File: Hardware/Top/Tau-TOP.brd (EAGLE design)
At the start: 38 x 38 mm, 64 parts, among them U3 PCF8523, U4 NRF52832_MODULE_MDBT42, U5 FT231XS

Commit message: Changes committed to top and bottom board
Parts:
- added J1: (no value), LinnesLab-Connectors:1X07
- moved C25 13.6 mm to (21.7, 36.0)
- moved R3 12.3 mm to (11.7, 17.0)
- moved C11 7.56 mm to (16.2, 24.9), turned to 270 degrees
- moved L2 7.42 mm to (15.5, 31.5)
- moved C9 5.77 mm to (23.6, 24.9)
- moved R4 5.77 mm to (11.0, 31.5), turned to 180 degrees
- moved C20 5.36 mm to (17.9, 25.1)
- moved C8 4.26 mm to (11.9, 24.8)
- moved C12 4.19 mm to (13.4, 24.8)
- moved C10 4.14 mm to (14.7, 24.8)
- moved C7 4.05 mm to (10.6, 24.8)
- moved XTAL2 2.28 mm to (25.1, 16.9)
- moved C21 1.47 mm to (18.7, 16.6)
- moved U2 0.26 mm to (19.1, 20.9)
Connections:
- removed net BATT: R13.1, R14.2
- removed net CD1: SD2.CD1
- removed net CHRG.STAT: CHRG2.1, R12.1
- removed net CS.OLED: U2.13
- removed net DC.OLED: U2.15
- removed net RESET.OLED: U2.14
- removed net SD.CS: SD2.2
- removed net SW1: U$1.A1, U$2.A1
- new net A4/BATT: R13.1, R14.2, U4.5
- new net A6/TIA: U4.7
- new net A7/PPG: U4.8
- new net D11/SW1: U$1.A1, U4.25
- new net D15/SW2: U$2.A1, U4.29
- new net D16/CS.OLED: U2.13, U4.30
- new net D27/CHRG.STATUS: CHRG2.1, R12.1, U4.4
- new net D29/LED.CTRL: U4.6
- new net D3/RESET.OLED: U2.14, U4.16
- new net D4/DC.OLED: U2.15, U4.17
- new net D5/CD1: SD2.CD1, U4.18
- new net D7/SD.CS: SD2.2, U4.20

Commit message: Changes made to top and bottom board
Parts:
- removed C22: (no value), LinnesLab-Passives:C0603
- removed C23, C24: 300p, LinnesLab-Passives:C0603
- removed C25: 10u, LinnesLab-Passives:C0805
- removed C26: 100n, LinnesLab-Passives:C0603
- removed CHRG2: MCP73831, LinnesLab-Power:SOT23-5
- removed D4, D5: (no value), LinnesLab-DiscreteSemi:USC
- removed JP2: (no value), LinnesLab-Switches:SMT-JUMPER_2_NO_SILK
- removed LDO2: MIC5504, LinnesLab-Power:SOT23-5
- removed LED5: RED, LinnesLab-LED:LED-0603
- removed LED6: YELLOW, LinnesLab-LED:LED-0603
- removed R19, R20: 1k, LinnesLab-Passives:R0603
- removed U$2: SWITCH.MOM, LinnesLab-Switches:TACTILE_SWITCH_SMD_6.2MM_TALL
- removed U5: FT231XS, LinnesLab-DigitalIC:SSOP20_L
- removed XTAL3: 32.7680kHz, LinnesLab-Clocks:2-SMD.NOLEAD.2.0MMTO1.2MM
- added C1, C18, C19: 1u, LinnesLab-Passives:C0603
- added C3: (no value), LinnesLab-Passives:C0603
- added C4: 10uF, LinnesLab-Passives:C0603
- added CHRG1: MCP73831, LinnesLab-Power:SOT23-5
- added D2, D3: (no value), LinnesLab-DiscreteSemi:USC
- added JP1: (no value), LinnesLab-Switches:SMT-JUMPER_2_NO_SILK
- added LDO1: MIC5504, LinnesLab-Power:SOT23-5
- added LED1: RED, LinnesLab-LED:LED-0603
- added LED2: BLUE, LinnesLab-LED:LED-0603
- added R16: 100k, LinnesLab-Passives:R0603
- added R7: 27, LinnesLab-Passives:R0603
- added SW1: (no value), LinnesLab-Switches:BUTTON-GULLWING
- added XTAL1: 32.768kHz, LinnesLab-Clocks:2-SMD.NOLEAD.2.0MMTO1.2MM
- C11, C12: value 2.2uF -> 300p; device LinnesLab-Passives:C0402 -> LinnesLab-Passives:C0603
- C13, C14: value 4.7u -> 47p
- C16: value 47p -> 4.7u
- C17: value 47p -> 100n
- C2: value 1u -> 10u; device LinnesLab-Passives:C0603 -> LinnesLab-Passives:C0805
- C21: value (none) -> 4.7u
- C5, C6: value 1u -> 2.2uF; device LinnesLab-Passives:C0603 -> LinnesLab-Passives:C0402
- C7: value 2.2uF -> (none); device LinnesLab-Passives:C0402 -> LinnesLab-Passives:C0603
- C9: value 10uF -> 2.2uF; device LinnesLab-Passives:C0603 -> LinnesLab-Passives:C0402
- J1: device LinnesLab-Connectors:1X07 -> LinnesLab-Connectors:1X07_1.27MM
- LED4: value BLUE -> YELLOW
- R1, R2: value 0 -> 10k
- R13: value 100k -> 1k
- R14, R15: value 100k -> 0
- R17: value 27 -> 100k
- R18: value 27 -> 1k
- R5, R6: value 10k -> 1k
- R8: value 1k -> 27
- R9: value 1k -> 100k
- SW3: value (none) -> SWITCH.MOM; device LinnesLab-Switches:BUTTON-GULLWING -> LinnesLab-Switches:TACTILE_SWITCH_SMD_6.2MM_TALL
- U4: value NRF52832_MODULE_MDBT42 -> FT231XS; device LinnesLab-Microcontrollers:BLE_MODULE_RAYTAC_MDBT42 -> LinnesLab-DigitalIC:SSOP20_L
- XTAL2: value 32.768kHz -> 32.7680kHz
- moved R6 66.4 mm to (41.3, 27.9), turned to 180 degrees
- moved R5 62.7 mm to (41.3, 25.9), turned to 180 degrees
- moved J1 62.6 mm to (5.00, 33.0)
- moved D1 55.8 mm to (12.8, -20.9), turned to 0 degrees
- moved R9 50.8 mm to (7.54, -11.4)
- moved C20 47.9 mm to (21.3, -22.7)
- moved R13 46.5 mm to (46.7, -12.2), turned to 0 degrees
- moved C2 42.6 mm to (21.7, 36.0), turned to 0 degrees
- moved XTAL2 42.6 mm to (31.8, -25.1), turned to 90 degrees
- moved U4 38.9 mm to (36.1, -9.35), turned to 90 degrees
- moved C16 37.9 mm to (5.00, -10.4), turned to 90 degrees
- moved SW3 37.8 mm to (22.2, 4.09)
- moved LED4 36.6 mm to (46.7, -8.43)
- moved R8 32.6 mm to (30.7, -5.51), turned to 0 degrees
- moved R15 30.9 mm to (-4.85, -20.1), turned to 0 degrees
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- renumbered CORTEX1 to DEBUG1, L2 to L1, SD2 to SD1, U$1 to SW2, USB2 to USB1
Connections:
- removed net FRST: U4.38
- net !CTS: now also JP1.2, U4.9; no longer JP2.2, U5.9
- net 3.3V: now also C17.2, C19.1, C2.2, C20.1, C9.2, D3.-, J1.4, LDO1.5, LED3.A, LED4.A, R1.2, R12.2, R2.2, U4.14, U4.3; no longer C12.2, C15.2, C2.1, C25.2, C6.1, D1.-, LDO2.5, LED5.A, LED6.A, R15.2, R5.2, R6.2, U4.11, U5.14, U5.3
- net A4/BATT: now also R16.1, R17.2; no longer R13.1, R14.2, U4.5
- net A6/TIA: now also J1.6; no longer U4.7
- net A7/PPG: now also J1.7; no longer U4.8
- net D11/SW1: no longer U4.25
- net D15/SW2: now also SW3.A1; no longer U$2.A1, U4.29
- net D16/CS.OLED: no longer U4.30
- net D27/CHRG.STATUS: now also CHRG1.1, R9.1; no longer CHRG2.1, R12.1, U4.4
- net D29/LED.CTRL: now also J1.5; no longer U4.6
- net D3/RESET.OLED: no longer U4.16
- net D4/DC.OLED: no longer U4.17
- net D5/CD1: no longer U4.18
- net D7/SD.CS: no longer U4.20
- net DFU: now also SW1.3; no longer SW3.3, U4.34
- net DTR: now also C15.1, U4.1; no longer C26.1, U5.1
- net FT3V3: now also U4.13; no longer U5.13
- net GND: now also C1.2, C11.2, C12.2, C13.1, C14.2, C16.1, C18.1, C19.2, C2.1, C21.2, C3.1, C4.1, C6.1, C7.2, CHRG1.2, J1.3, JP1.1, LDO1.2, LED1.C, LED2.C, R12.1, R17.1, SW1.1, SW3.B1, SW3.B2, U4.16, U4.6; no longer C11.1, C12.1, C13.2, C14.1, C15.1, C16.2, C2.2, C21.1, C22.2, C23.2, C24.2, C25.1, C5.1, C6.2, CHRG2.2, JP2.1, LDO2.2, LED3.C, LED4.C, R14.1, R15.1, SW3.1, U$2.B1, U$2.B2, U4.1, U4.12, U4.24, U4.39, U5.16, U5.6
- net LED1: now also R5.2; no longer R8.2, U4.31
- net LED2: now also R6.2; no longer R9.2, U4.33
- net MISO: no longer U4.28
- net MOSI: no longer U4.27
- net N$10: now also CHRG1.5; no longer CHRG2.5
- net N$12: now also XTAL2.P$1; no longer XTAL3.P$1
- net N$13: now also XTAL2.P$2; no longer XTAL3.P$2
- net N$16: now also C3.2, XTAL1.P$1; no longer C21.2, U4.13, XTAL2.P$1
- net N$17: now also C7.1, XTAL1.P$2; no longer C22.1, U4.14, XTAL2.P$2
- net N$18: now also LED1.A, R5.1; no longer LED3.A, R8.1
- net N$19: now also LED2.A, R6.1; no longer LED4.A, R9.1
- net N$20: no longer U4.10
- net N$21: now also C1.1; no longer C20.1, U4.9
- net N$22: now also R7.2, U4.12; no longer R17.2, U5.12
- net N$24: now also R8.2, U4.11; no longer R18.2, U5.11
- net N$25: now also LED3.C, R13.2; no longer LED5.C, R19.2
- net N$26: now also LED4.C, R18.2; no longer LED6.C, R20.2
- net N$3: now also C8.2; no longer C7.2
- net N$4: now also C8.1; no longer C7.1
- net N$5: now also C5.2; no longer C8.2
- net N$6: now also C5.1; no longer C8.1
- net N$7: now also C4.2; no longer C9.2
- net N$8: now also C6.2; no longer C11.2
- net P0.09/NFC1: now also C11.1; no longer C24.1, U4.22
- net P0.10/NFC2: now also C12.1; no longer C23.1, U4.23
- net RESET: now also C15.2, D3.+; no longer C26.2, D1.+, U4.35
- net RXD.FT: now also R15.1, U4.4; no longer R2.1, U5.4
- net RXD.NRF: now also R14.2; no longer R1.2, U4.21
- net RXLED: now also R13.1, U4.17; no longer R19.1, U5.17
- net SCK: no longer U4.26
- net SCL: now also J1.2, R2.1; no longer R6.1, U4.3
- net SDA: now also J1.1, R1.1; no longer R5.1, U4.2
- net SWCLK: no longer U4.36
- net SWDIO: no longer U4.37
- net SWO: no longer U4.32
- net TXD.FT: now also R14.1, U4.20; no longer R1.1, U5.20
- net TXD.NRF: now also R15.2; no longer R2.2, U4.19
- net TXLED: now also R18.1, U4.10; no longer R20.1, U5.10
- net USB+: now also C14.1, R8.1; no longer C16.1, R18.1
- net USB-: now also C13.2, R7.1; no longer C17.2, R17.1
- net VIN: now also C16.2, C18.2, CHRG1.4, D1.-, D2.-, LDO1.1, LDO1.3, R9.2; no longer C14.2, C5.2, CHRG2.4, D4.-, D5.-, LDO2.1, LDO2.3, R12.2
- net VLIPO: now also C21.1, CHRG1.3, D1.+, R16.2; no longer C13.1, CHRG2.3, D4.+, R13.2
- net V_USB: now also D2.+, U4.15; no longer D5.+, U5.15
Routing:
- net N$13: track 0.00 -> 2.00 mm
- net N$12: track 0.00 -> 1.96 mm
- added copper zone on layer 16, net GND

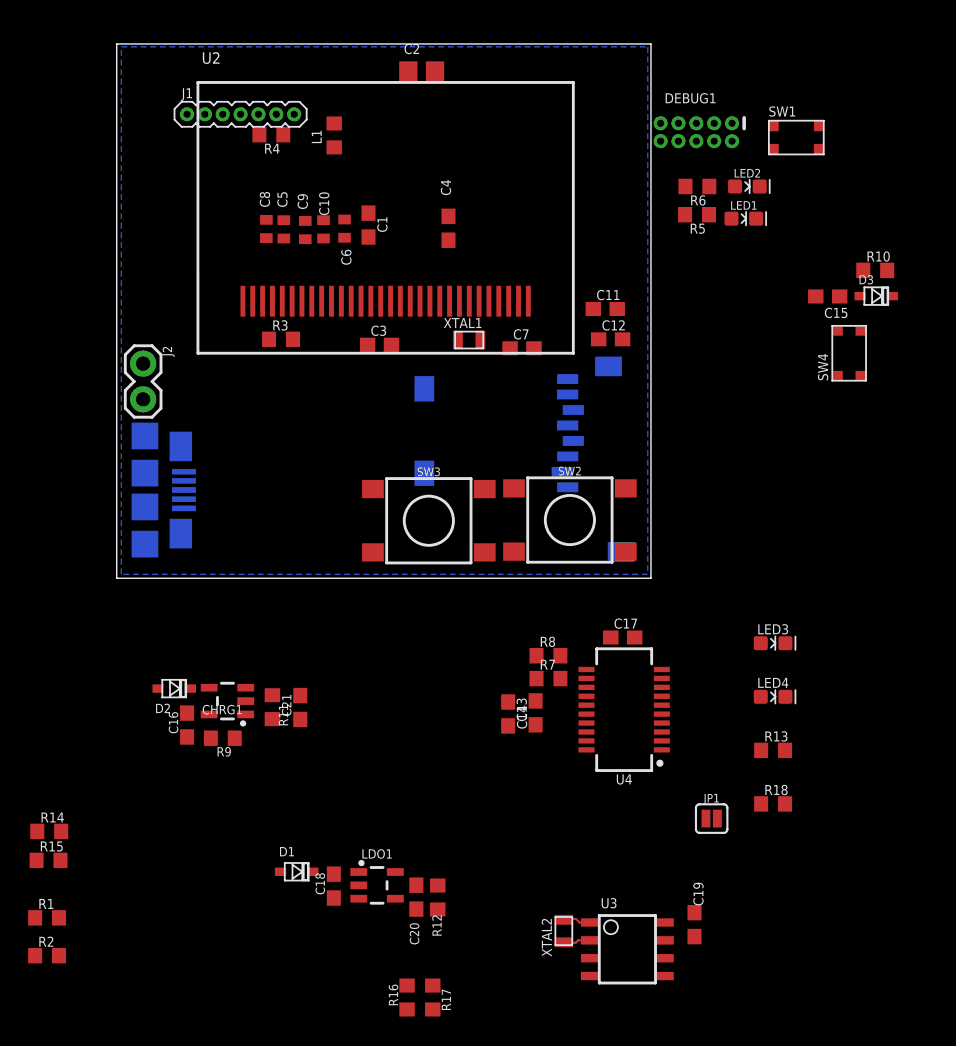
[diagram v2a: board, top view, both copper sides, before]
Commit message: Changes made to Top board and arduino files
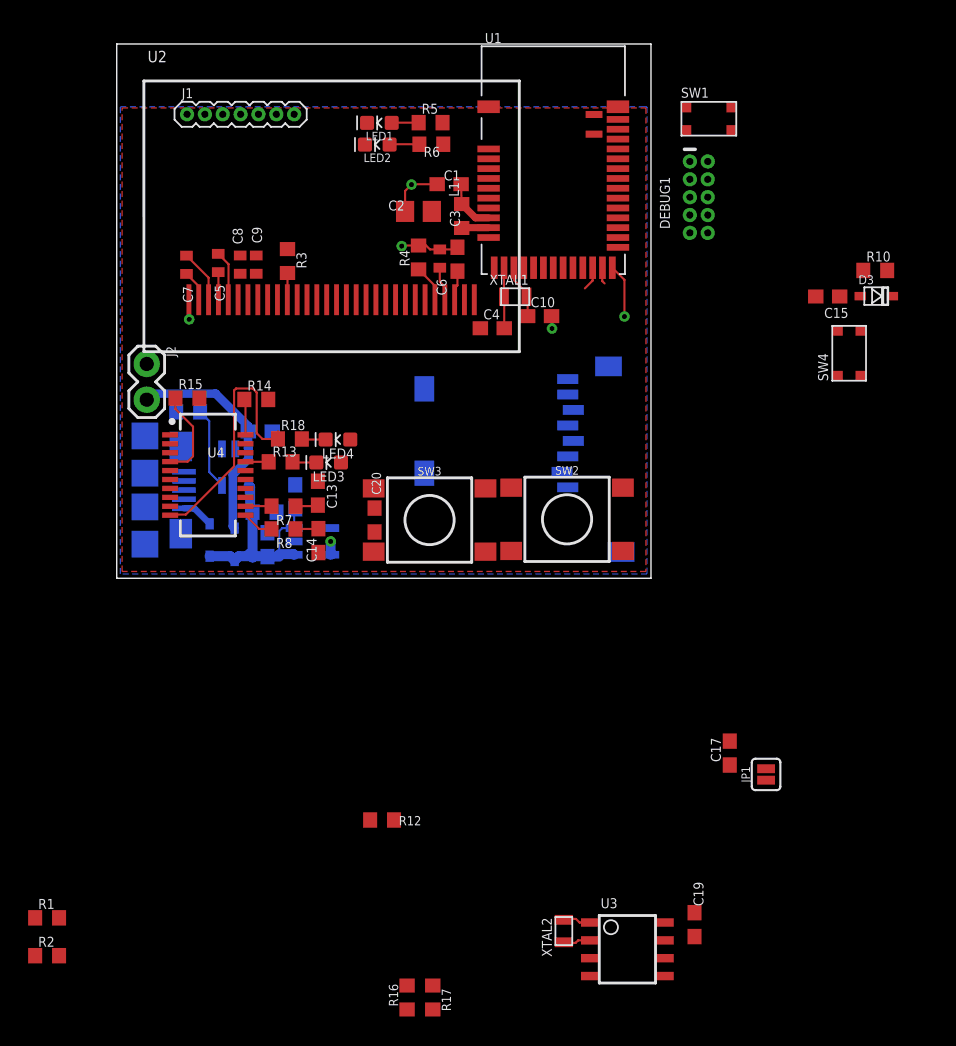
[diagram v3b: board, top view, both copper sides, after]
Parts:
- removed C11, C12: 300p, LinnesLab-Passives:C0603
- added U1: NRF52832_MODULE_MDBT42, LinnesLab-Microcontrollers:BLE_MODULE_RAYTAC_MDBT42
- C10: value 2.2uF -> (none); device LinnesLab-Passives:C0402 -> LinnesLab-Passives:C0603
- C3: value (none) -> 10uF
- C4: value 10uF -> (none)
- C7: value (none) -> 2.2uF; device LinnesLab-Passives:C0603 -> LinnesLab-Passives:C0402
- moved R18 43.1 mm to (12.3, 9.91)
- moved R13 40.6 mm to (11.7, 8.28)
- moved LED4 36.0 mm to (15.7, 9.87), turned to 180 degrees
- moved R15 34.3 mm to (5.03, 12.8)
- moved LED3 34.1 mm to (15.1, 8.23), turned to 180 degrees
- moved R14 34.1 mm to (9.93, 12.7)
- moved U4 34.0 mm to (6.48, 7.34), turned to 270 degrees
- moved C20 27.0 mm to (18.3, 4.14), turned to 90 degrees
- moved LED1 26.8 mm to (18.7, 32.4), turned to 180 degrees
- moved LED2 26.5 mm to (18.5, 30.8), turned to 180 degrees
- moved LDO1 24.9 mm to (13.9, 2.62), flipped to the bottom, turned to 90 degrees
- moved C18 24.7 mm to (10.7, 2.39), flipped to the bottom, turned to 270 degrees
- moved C7 24.6 mm to (4.96, 22.3), turned to 270 degrees
- moved D1 23.7 mm to (8.38, 2.41), flipped to the bottom, turned to 270 degrees
- moved R7 22.5 mm to (11.9, 5.13), turned to 180 degrees
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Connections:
- removed net N$16: C3.2, XTAL1.P$1
- removed net N$17: C7.1, XTAL1.P$2
- removed net N$20: L1.1
- removed net N$21: C1.1, L1.2
- new net FRST: U1.38
- new net N$31: C4.2, U1.13, XTAL1.P$1
- new net N$32: C10.1, U1.14, XTAL1.P$2
- new net N$35: L1.1, U1.10
- new net N$36: C1.1, L1.2, U1.9
- new net RXD: U1.21
- new net TXD: U1.19
- net 3.3V: now also C8.2, U1.11; no longer C10.2
- net DFU: now also U1.34
- net GND: now also C10.2, C8.1, U1.1, U1.12, U1.24, U1.39; no longer C10.1, C11.2, C12.2, C7.2, SW2.B2, SW3.B2
- net LED1: now also U1.31
- net LED2: now also U1.33
- net MISO: now also U1.28
- net MOSI: now also U1.27
- net N$3: now also C7.2; no longer C8.2
- net N$4: now also C7.1; no longer C8.1
- net N$7: now also C3.2; no longer C4.2
- net P0.09/NFC1: now also U1.22; no longer C11.1
- net P0.10/NFC2: now also U1.23; no longer C12.1
- net RESET: now also U1.35
- net SCK: now also U1.26
- net SCL: now also U1.3
- net SDA: now also U1.2
- net SWCLK: now also U1.36
- net SWDIO: now also U1.37
- net SWO: now also U1.32
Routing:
- net TXLED: track 0.00 -> 18.3 mm
- net VLIPO: track 0.00 -> 16.4 mm
- net VIN: track 0.00 -> 16.3 mm
- net GND: track 0.00 -> 14.3 mm, vias 0 -> 5
- net RXD.FT: track 0.00 -> 6.45 mm
- net N$10: track 0.00 -> 5.88 mm
- net N$31: track 0.00 -> 4.32 mm
- net N$32: track 0.00 -> 4.14 mm
- net N$4: track 0.00 -> 3.79 mm
- net N$36: track 0.00 -> 3.73 mm
- net N$6: track 0.00 -> 3.57 mm
- net N$2: track 0.00 -> 2.67 mm
- net TXD.FT: track 0.00 -> 2.59 mm
- net N$8: track 0.00 -> 2.47 mm
- net V_USB: track 0.00 -> 2.29 mm
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- added copper zone on layer 1, net 3.3V

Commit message: Changes made to top and bottom board
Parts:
- removed C19, C20: 1u, LinnesLab-Passives:C0603
- removed C21: 4.7u, LinnesLab-Passives:C0603
- removed SD1: (no value), LinnesLab-Connectors:MICROSD
- removed U3: PCF8523, LinnesLab-Clocks:SO8
- removed XTAL2: 32.7680kHz, LinnesLab-Clocks:2-SMD.NOLEAD.2.0MMTO1.2MM
- added C11, C12: 1u, LinnesLab-Passives:C0603
- C18: value 1u -> 4.7u
- moved R2 62.1 mm to (18.0, 30.8), turned to 180 degrees
- moved R1 60.9 mm to (18.0, 32.3), turned to 180 degrees
- moved C17 52.1 mm to (14.5, 30.8), turned to 0 degrees
- moved R17 48.2 mm to (6.53, 15.6), turned to 90 degrees
- moved R16 48.1 mm to (4.83, 15.6), turned to 270 degrees
- moved R12 47.9 mm to (1.80, 27.5), turned to 270 degrees
- moved JP1 46.7 mm to (2.50, 2.63)
- moved LDO1 31.4 mm to (2.72, 31.9), flipped to the top, turned to 0 degrees
- moved C18 28.8 mm to (4.85, 30.6), flipped to the top
- moved R9 24.1 mm to (5.94, 28.3), flipped to the top
- moved R10 21.6 mm to (34.7, 12.0), turned to 180 degrees
- moved C16 20.9 mm to (2.49, 24.0), flipped to the top, turned to 180 degrees
- moved D3 20.3 mm to (34.8, 13.7), turned to 180 degrees
- moved LED2 20.0 mm to (35.5, 20.3), turned to 270 degrees
- moved LED1 19.1 mm to (33.4, 20.2), turned to 270 degrees
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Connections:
- removed net A4/BATT: R16.1, R17.2
- removed net A6/TIA: J1.6
- removed net A7/PPG: J1.7
- removed net CD2: SD1.CD2
- removed net D29/LED.CTRL: J1.5
- removed net D5/CD1: SD1.CD1
- removed net D7/SD.CS: SD1.2
- removed net N$12: U3.2, XTAL2.P$1
- removed net N$13: U3.1, XTAL2.P$2
- removed net RXD: U1.21
- removed net TXD: U1.19
- removed net VBAT: U3.3
- new net A4/PPG: J1.7, U1.5
- new net A5/TIA: J1.5, U1.6
- new net A7/BATT: R16.1, R17.2, U1.8
- new net D30/LED.CTRL: J1.6, U1.7
- new net VIN1: C11.2, C18.2, CHRG1.4, LDO1.1, LDO1.3, R9.2
- net 3.3V: now also C12.1; no longer C19.1, C20.1, SD1.4, U3.8
- net D11/SW1: now also U1.25
- net D15/SW2: now also U1.29
- net D16/CS.OLED: now also U1.30
- net D27/CHRG.STATUS: now also U1.4
- net D3/RESET.OLED: now also U1.16
- net D4/DC.OLED: now also U1.17
- net GND: now also C11.1, C12.2, C16.2; no longer C16.1, C19.2, C20.2, C21.2, SD1.6, SD1.MT1, SD1.MT2, U3.4
- net MISO: no longer SD1.7
- net MOSI: no longer SD1.3
- net RXD.NRF: now also U1.21
- net SCK: no longer SD1.5
- net SCL: no longer U3.6
- net SDA: no longer U3.5
- net TXD.NRF: now also U1.19
- net VIN: no longer C16.2, C18.2, CHRG1.4, LDO1.1, LDO1.3, R9.2
- net VLIPO: now also C16.1; no longer C21.1
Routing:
- net GND: track 14.3 -> 63.9 mm, vias 5 -> 32
- net DTR: track 0.00 -> 36.4 mm, vias 0 -> 4
- net TXD.NRF: track 0.00 -> 28.4 mm, vias 0 -> 2
- net D27/CHRG.STATUS: track 0.00 -> 26.2 mm, vias 0 -> 2
- net RESET: track 0.00 -> 26.0 mm, vias 0 -> 1
- net A7/BATT: track 0.00 -> 24.7 mm, vias 0 -> 2
- net D15/SW2: track 0.00 -> 22.7 mm, vias 0 -> 2
- net D16/CS.OLED: track 0.00 -> 22.6 mm, vias 0 -> 2
- net RXD.NRF: track 0.00 -> 22.4 mm, vias 0 -> 3
- net SCK: track 0.00 -> 20.0 mm, vias 0 -> 2
- net D11/SW1: track 0.00 -> 19.8 mm
- net MOSI: track 0.00 -> 19.2 mm, vias 0 -> 2
- net SDA: track 0.00 -> 19.1 mm, vias 0 -> 2
- net VLIPO: track 16.4 -> 34.6 mm, vias 0 -> 1
- net SCL: track 0.00 -> 18.0 mm
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
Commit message: Finished Bottom and Top boards' first version
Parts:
- C11, C12: value 1u -> 47p
- C13: value 47p -> 100n
- C14: value 47p -> 4.7u
- C16: value 4.7u -> 1u
- C17: value 100n -> 1u
- moved C14 29.3 mm to (4.85, 30.6)
- moved C12 26.9 mm to (13.5, 2.58), turned to 270 degrees
- moved C15 25.6 mm to (14.5, 30.8)
- moved C11 25.6 mm to (13.5, 5.95)
- moved C13 23.4 mm to (34.9, 15.3), turned to 0 degrees
- moved C17 11.6 mm to (3.40, 27.5), turned to 90 degrees
- moved C16 7.75 mm to (6.63, 30.6), turned to 270 degrees
- moved C18 6.99 mm to (2.49, 24.0), turned to 180 degrees
- renumbered SW4 to RESET, U4 to U3
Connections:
- net 3.3V: now also C15.2, C17.1; no longer C12.1, C17.2
- net DTR: now also C13.1; no longer C15.1
- net GND: now also C14.1, C15.1, C16.1, C17.2, C18.2; no longer C13.1, C14.2, C16.2, C17.1, C18.1
- net RESET: now also C13.2; no longer C15.2
- net USB+: now also C12.1; no longer C14.1
- net USB-: now also C11.2; no longer C13.2
- net VIN1: now also C14.2, C16.2; no longer C11.2, C18.2
- net VLIPO: now also C18.1; no longer C16.1
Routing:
- net GND: track 63.9 -> 65.9 mm, vias 32 -> 34
- net RXD.NRF: vias 3 -> 2
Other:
- board text added: "+"
